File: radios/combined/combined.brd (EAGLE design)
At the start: 21.5 x 31.4 mm, 14 parts

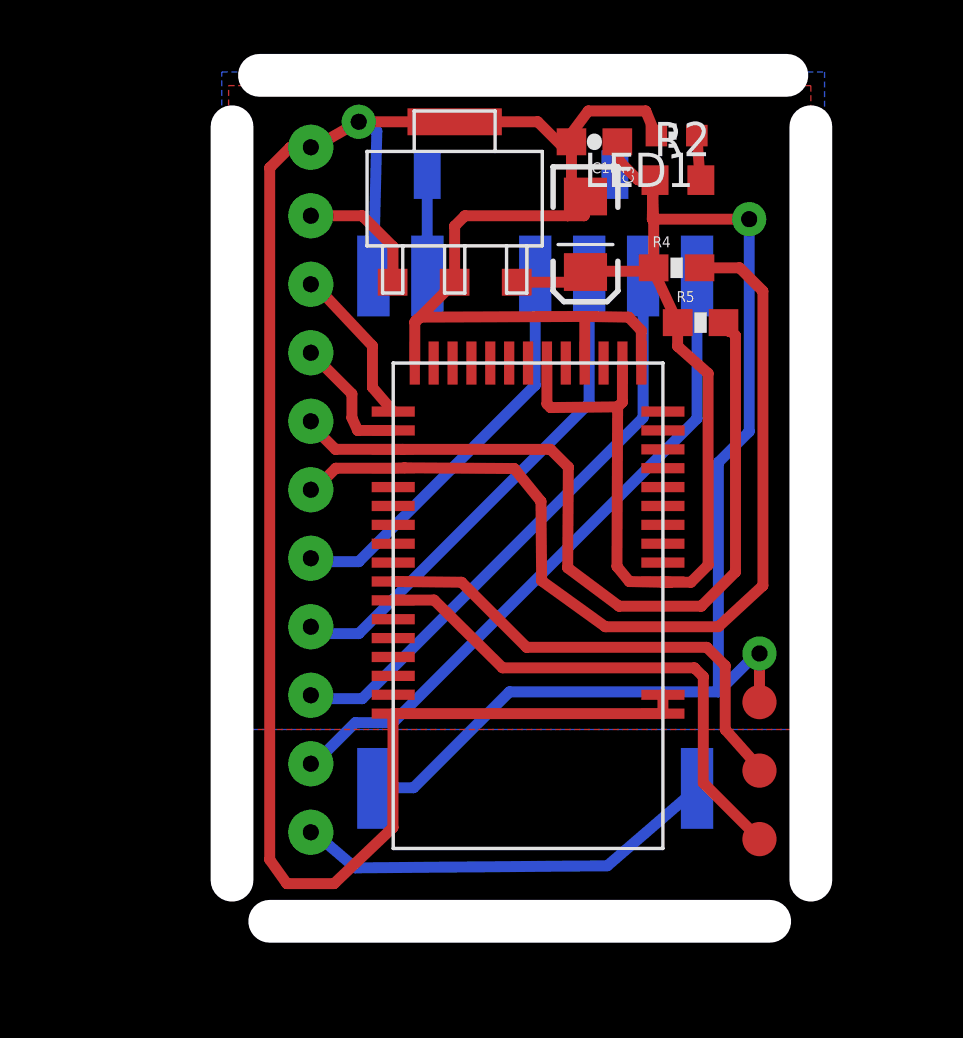
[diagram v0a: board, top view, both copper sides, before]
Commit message: updated so nrf51 uses SPI instead of UART
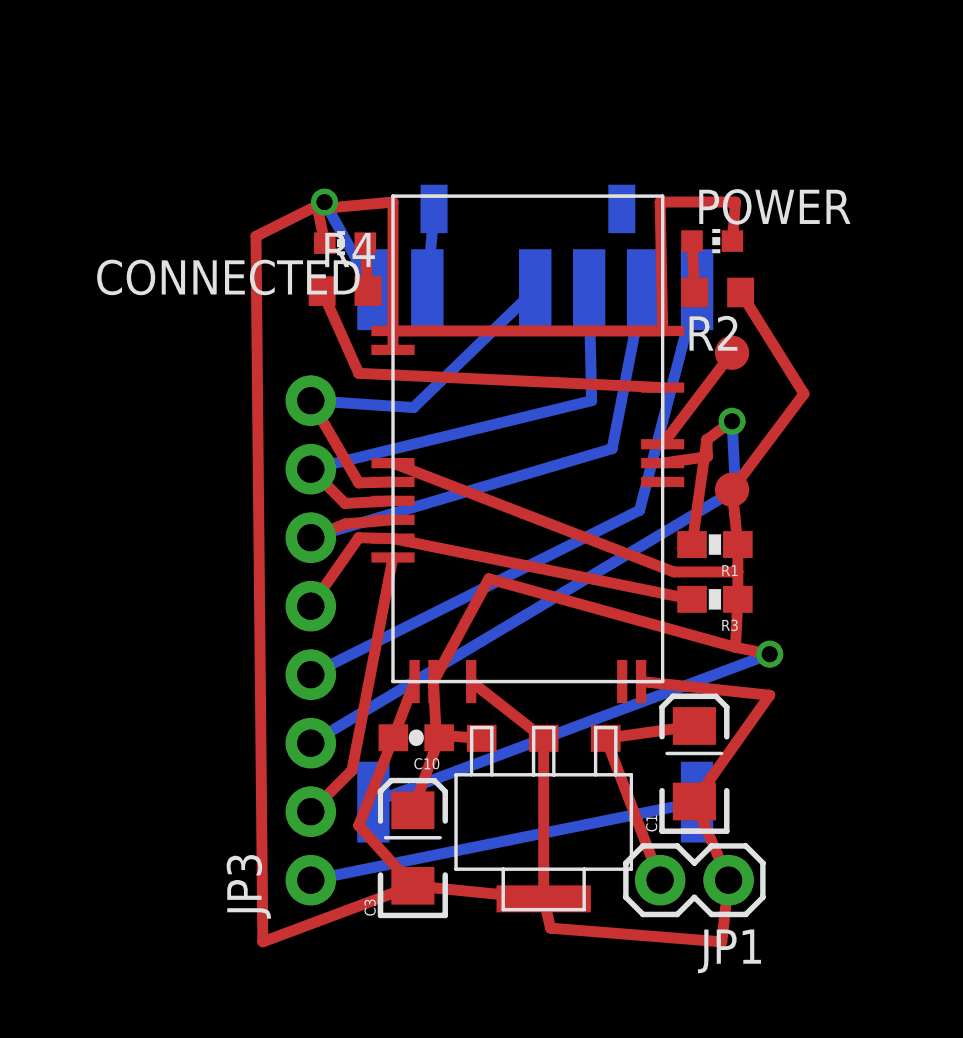
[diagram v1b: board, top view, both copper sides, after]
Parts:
- removed DATA: PAD, ITP_Lab:SMD-ROUND
- removed LED1: (no value), adafruit:CHIP-LED0603
- removed R5: 100k, SparkFun-Resistors:0603-RES
- removed U$4: MDBT40, ITP_Lab:MDBT40
- added C1: 10uF, SparkFun-Capacitors:EIA3216
- added CONNECTED, POWER: (no value), adafruit:CHIP-LED0603
- added JP1: M02PTH, SparkFun-Connectors:1X02
- added JP3: (no value), SparkFun-Connectors:1X08_NO_SILK
- added R1, R3: 10k, SparkFun-Resistors:0603-RES
- C10: value 0.1uF -> 1uF
- R2: value (none) -> 10k
- R4: value 100k -> 10k; device SparkFun-Resistors:0603-RES -> adafruit:R0603
- U$5: value HEADER-11 -> NRF51-MDBT40-SPI; device ITP_Lab:HEADER-11 -> ITP_Lab:SOC-NRF51-MDBT40-SPI
- moved C3 23.6 mm to (6.32, 1.96), turned to 90 degrees
- moved U$3 23.3 mm to (11.2, 2.92), turned to 180 degrees
- moved C10 23.1 mm to (6.45, 6.05)
- moved CLOCK 18.1 mm to (18.2, 20.3), turned to 180 degrees
- moved R4 12.3 mm to (3.81, 22.6)
- moved U$5 8.14 mm to (10.7, 15.7), turned to 0 degrees
- moved VCC 7.94 mm to (18.2, 15.2), turned to 180 degrees
- moved R2 4.42 mm to (17.6, 22.6), turned to 180 degrees
- moved U$2 1.30 mm to (10.6, 25.7)
- moved U$1 0.51 mm to (11.9, 13.2)
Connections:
- removed net BT-CTS: R5.2, U$4.P0.10, U$5.5
- removed net BT-RTS: U$4.P0.08, U$5.3
- removed net BT-RX: R4.2, U$4.P0.11, U$5.6
- removed net BT-TX: U$4.P0.09, U$5.4
- removed net N$12: DATA.P$1, U$4.SWDIO
- new net BT-REQ: JP3.2, U$5.P0.25
- new net BT-SS: JP3.5, R3.2, U$5.P0.24
- new net N$2: R4.1, U$5.P0.19
- new net N$4: CONNECTED.A, R4.2
- new net SWDIO/RST: JP3.3, R1.2, U$5.SWDIO
- net GND: now also C1.C, CONNECTED.C, JP1.1, POWER.C, U$5.GND1, U$5.GND2, U$5.GND3, U$5.GND4, U$5.GND5, U$5.P0.30; no longer LED1.C, U$4.GND1, U$4.GND2, U$4.GND3, U$4.GND4, U$4.GND5, U$4.P0.30, U$5.1
- net MISO: now also JP3.7, U$5.P0.22; no longer U$5.8
- net MOSI: now also JP3.6, U$5.P0.23; no longer U$5.9
- net N$1: now also POWER.A; no longer LED1.A
- net N$11: now also U$5.SWCLK; no longer U$4.SWCLK
- net RF-REQ: now also JP3.1; no longer U$5.11
- net RF-SS: now also JP3.4; no longer U$5.10
- net SCK: now also JP3.8, U$5.P0.21; no longer U$5.7
- net VCC: now also R1.1, R3.1, U$5.AVDD, U$5.VDD; no longer R4.1, R5.1, U$4.AVDD, U$4.P0.01, U$4.VDD
- net VIN: now also C1.A, JP1.2; no longer U$5.2
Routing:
- net BT-RX: track 35.4 -> 0.00 mm
- net BT-CTS: track 30.7 -> 0.00 mm
- net SWDIO/RST: track 0.00 -> 28.3 mm, vias 0 -> 1
- net N$12: track 17.9 -> 0.00 mm
- net GND: track 95.5 -> 113.2 mm
- net BT-SS: track 0.00 -> 15.7 mm
- net N$11: track 19.6 -> 4.26 mm
- net N$2: track 0.00 -> 14.6 mm
- net VCC: track 79.2 -> 65.8 mm, vias 2 -> 1
- net BT-REQ: track 0.00 -> 10.2 mm
- net BT-RTS: track 5.99 -> 0.00 mm
- net BT-TX: track 4.88 -> 0.00 mm
- net VIN: track 4.85 -> 8.95 mm
- net RF-SS: track 24.9 -> 22.1 mm
- net N$4: track 0.00 -> 1.78 mm
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- removed copper zone on layer 1, net GND
- removed copper zone on layer 16, net GND
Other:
- board outline removed

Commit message: SPI combined board ready to print
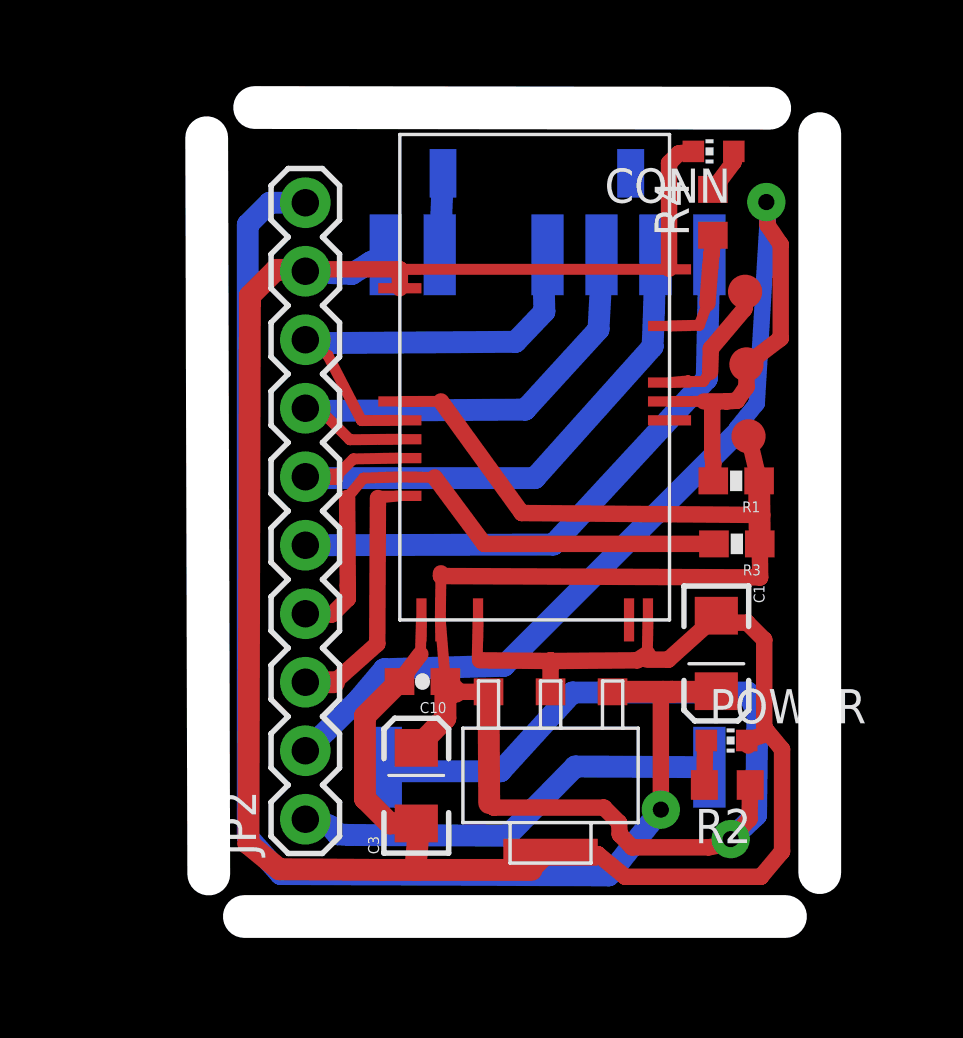
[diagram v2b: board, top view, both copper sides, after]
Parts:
- removed CONNECTED: (no value), adafruit:CHIP-LED0603
- removed JP1: M02PTH, SparkFun-Connectors:1X02
- removed JP3: (no value), SparkFun-Connectors:1X08_NO_SILK
- added CLOCK1: PAD, ITP_Lab:SMD-ROUND
- added CONN: (no value), adafruit:CHIP-LED0603
- added JP2: M10", SparkFun-Connectors:1X10
- moved POWER 18.5 mm to (18.0, 5.94)
- moved R2 18.3 mm to (18.0, 4.29)
- moved R4 13.9 mm to (17.4, 25.5), turned to 90 degrees
- moved C1 4.17 mm to (17.6, 9.17), turned to 270 degrees
- moved R1 2.49 mm to (18.3, 15.6)
- moved C3 2.31 mm to (6.45, 4.27)
- moved CLOCK 2.31 mm to (18.6, 22.6)
- moved U$5 2.30 mm to (10.9, 18.0)
- moved R3 2.21 mm to (18.3, 13.2)
- moved C10 2.10 mm to (6.68, 8.13)
- moved VCC 2.07 mm to (18.8, 17.2)
- moved U$3 1.75 mm to (11.4, 4.65)
- moved U$1 1.37 mm to (12.3, 14.5)
- moved U$2 1.36 mm to (10.9, 27.0)
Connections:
- net BT-REQ: now also JP2.3; no longer JP3.2
- net BT-SS: now also JP2.4; no longer JP3.5
- net GND: now also CONN.C, JP2.9; no longer CONNECTED.C, JP1.1
- net MISO: now also JP2.7; no longer JP3.7
- net MOSI: now also JP2.6; no longer JP3.6
- net N$4: now also CONN.A; no longer CONNECTED.A
- net RF-REQ: now also JP2.1; no longer JP3.1
- net RF-SS: now also JP2.5; no longer JP3.4
- net SCK: now also JP2.8; no longer JP3.8
- net SWDIO/RST: now also CLOCK1.P$1, JP2.2; no longer JP3.3
- net VIN: now also JP2.10; no longer JP1.2
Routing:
- net VIN: track 8.95 -> 51.5 mm, vias 0 -> 1
- net SWDIO/RST: track 28.3 -> 43.6 mm
- net VCC: track 65.8 -> 78.4 mm
- net N$2: track 14.6 -> 4.57 mm
- net GND: track 113.2 -> 103.4 mm, vias 1 -> 0
- net BT-SS: track 15.7 -> 20.8 mm
- net SCK: track 14.9 -> 16.7 mm
- net RF-REQ: track 14.6 -> 16.3 mm
- net MOSI: track 20.8 -> 22.3 mm
- net N$11: track 4.26 -> 5.13 mm
- net BT-REQ: track 10.2 -> 9.59 mm
- net MISO: track 18.4 -> 19.0 mm
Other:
- board outline added: 22.7 x 30 mm

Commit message: replaced chip antenna with pad for wire
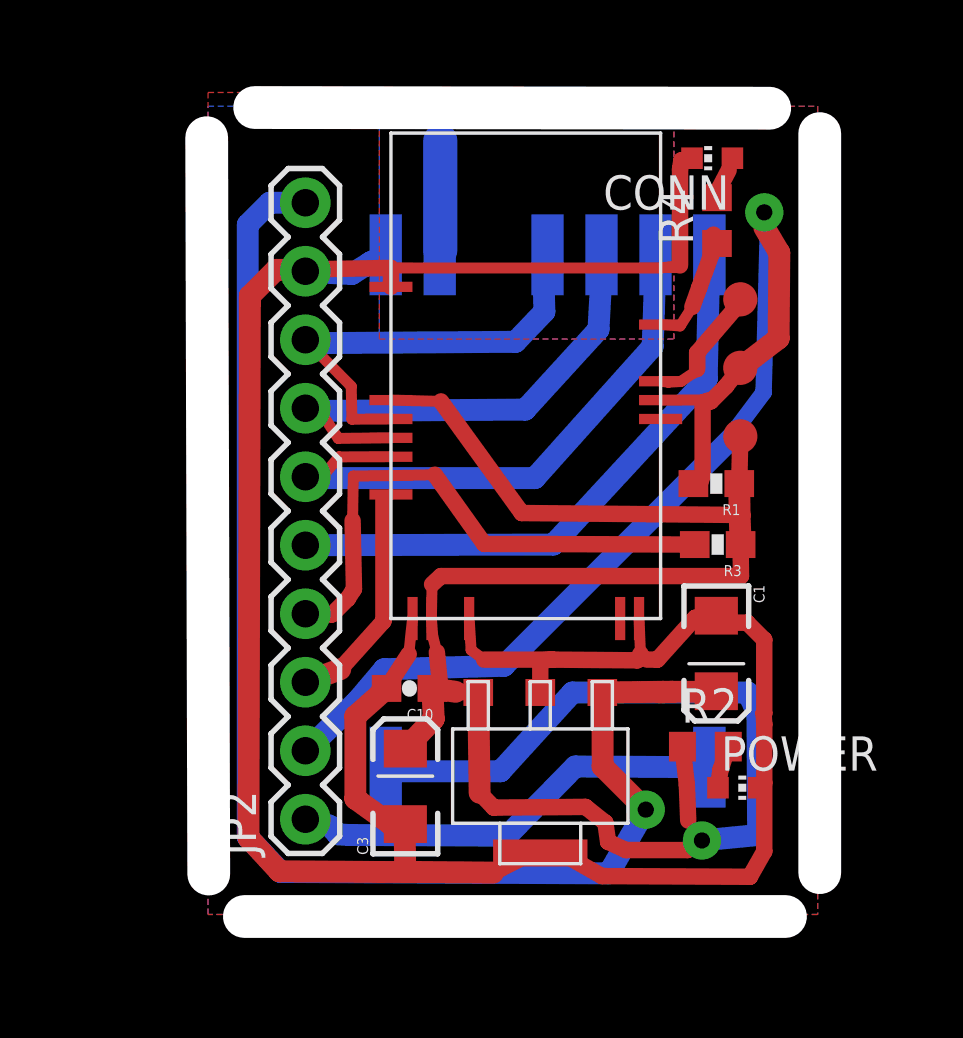
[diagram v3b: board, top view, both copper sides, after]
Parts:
- removed U$2: 915MHZ-ANTENNA-SMD, ITP_Lab:915MHZ-ANTENNA
- moved POWER 1.81 mm to (18.4, 4.19)
- moved R2 1.64 mm to (17.2, 5.71), turned to 0 degrees
- moved R1 0.74 mm to (17.6, 15.5)
- moved R3 0.71 mm to (17.6, 13.2)
- moved C10 0.55 mm to (6.20, 7.87)
- moved C3 0.41 mm to (6.05, 4.24)
- moved U$3 0.38 mm to (11.0, 4.62)
- moved R4 0.34 mm to (17.6, 25.2)
- moved U$5 0.33 mm to (10.6, 18.1)
- moved CLOCK 0.33 mm to (18.5, 22.3)
- moved VCC 0.30 mm to (18.5, 17.2)
- moved CLOCK1 0.26 mm to (18.5, 19.8)
- moved CONN 0.26 mm to (17.4, 27.5)
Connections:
- removed net N$6: U$1.ANT, U$2.SIGNAL
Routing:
- net VIN: track 51.5 -> 54.3 mm
- net GND: track 103.4 -> 101.9 mm
- net N$6: track 3.02 -> 4.06 mm
- net VCC: track 78.4 -> 79.4 mm
- net BT-REQ: track 9.59 -> 8.81 mm
- added copper zone on layer 1, net GND
- added copper zone on layer 16, net GND
